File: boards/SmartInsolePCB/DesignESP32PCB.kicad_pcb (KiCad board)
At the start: 2 copper layers, 54 parts, among them J1 Conn_01x02_Pin, J10 Conn_01x02_Pin, J11 Conn_01x02_Pin, J12 Conn_01x02_Pin, J2 Conn_01x02_Pin, J3 Conn_01x06_Pin, J4 Conn_01x02_Pin, J5 Conn_01x02_Pin, J6 Conn_01x02_Pin, J7 Conn_01x02_Pin, J8 Conn_01x02_Pin, J9 Conn_01x02_Pin, SW1 SW_Push, SW2 SW_Push, U1 ESP32-S3-MINI-1-N8, U2 D3V3XA4B10LP, U3 TLV75801PDRV, U4 SN74LVC1G14DBV, U5 SN74LVC1G14DBV, U6 MPU-6050

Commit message: finished schematic
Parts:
- added SW3: SW_Push, Button_Switch_SMD:SW_Push_1P1T_NO_CK_PTS125Sx43PSMTR, F.Cu at (49.2, 75.9)
- added SW4: SW_Push, Button_Switch_SMD:SW_Push_1P1T_NO_CK_PTS125Sx43PSMTR, F.Cu at (49.2, 89.4)
- added U7: ESP32-S3-WROOM-1, RF_Module:ESP32-S3-WROOM-1, F.Cu at (186.1, 62.7)
- BOOT1, RESET1: footprint Button_Switch_SMD:SW_SPST_PTS810 -> Button_Switch_SMD:SW_Push_1P1T_NO_CK_PTS125Sx43PSMTR
- C5, C8: value 0.1uF -> 1uF
- J3: value Conn_01x06_Pin -> PJS008U-3000-0; footprint Connector_PinHeader_1.00mm:PinHeader_1x06_P1.00mm_Vertical -> SmartInsolePCB:PJS008U30000
- R14, R15: value 1k -> 10k
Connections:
- C5 pad 1: Net-(C5-Pad1) -> /End Hike
- C8 pad 1: Net-(C8-Pad1) -> /Start Hike
- J3 pad 1: GND -> /CS
- J3 pad 2: /GPIO48 -> /MOSI
- J3 pad 3: /GPIO45 -> GND
- J3 pad 4: /GPIO47 -> /3V3
- J3 pad 5: /CS -> /SCLK
- J3 pad 6: +3.3V -> GND
- R10 pad 1: /GPIO12 -> /GPIO3
- R11 pad 1: /GPIO13 -> /GPIO6
- R12 pad 1: /GPIO14 -> /GPIO7
- R13 pad 1: /GPIO15 -> /GPIO8
- R14 pad 2: +3.3V -> /End Hike
- R15 pad 1: Net-(C8-Pad1) -> Net-(R15-Pad1)
- R15 pad 2: Net-(R14-Pad1) -> /Start Hike
- R18 pad 1: /GPIO16 -> /GPIO11
- R19 pad 1: /GPIO17 -> /GPIO12
- R20 pad 1: /GPIO18 -> /GPIO21
- R21 pad 1: /GPIO19 -> /GPIO38
- R22 pad 1: /GPIO20 -> /GPIO47
- R3 pad 1: /GPIO10 -> /GPIO1
- R9 pad 1: /GPIO11 -> /GPIO2
- SW1 pad 2: Net-(R16-Pad1) -> Net-(R14-Pad1)
- SW2 pad 2: Net-(R14-Pad1) -> Net-(R15-Pad1)
- U6 pad 23: /GPIO35 -> /SCL_6050
- U6 pad 24: /GPIO34 -> /SDA_6050

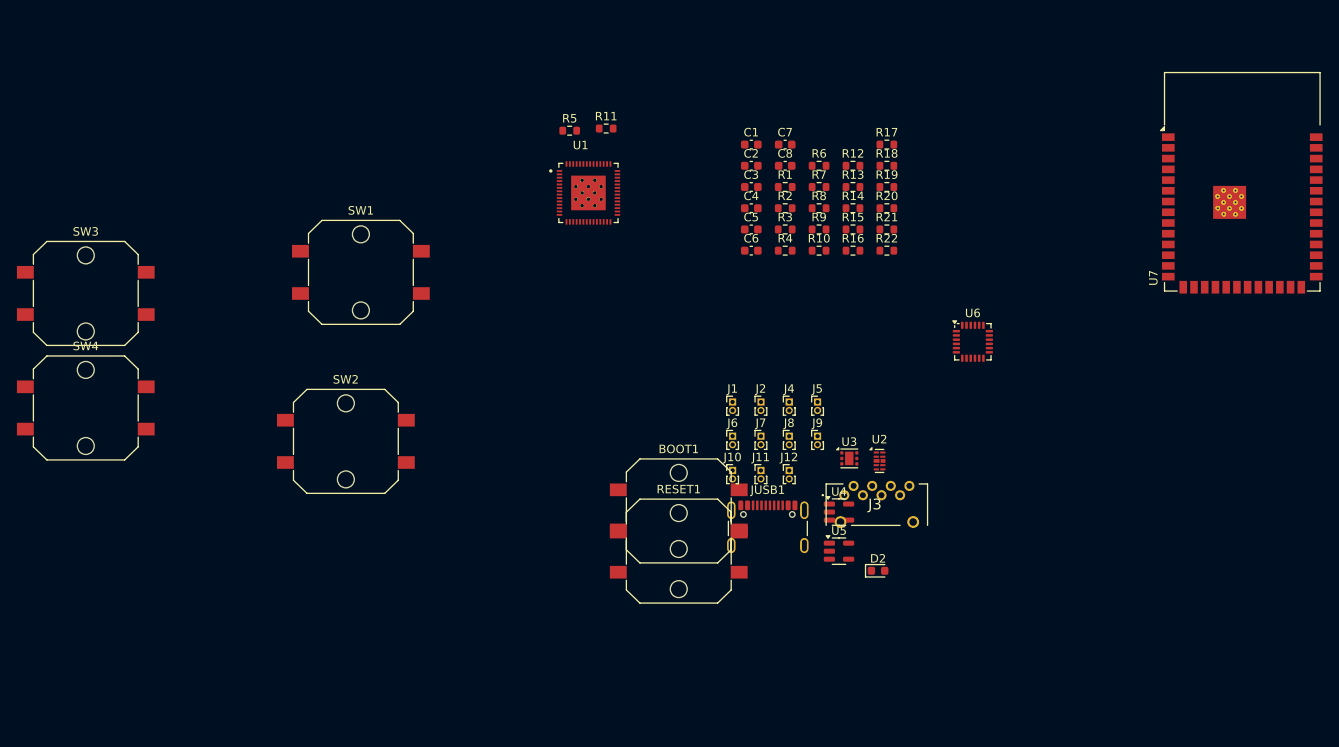
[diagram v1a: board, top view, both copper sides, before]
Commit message: finished all PCB connections
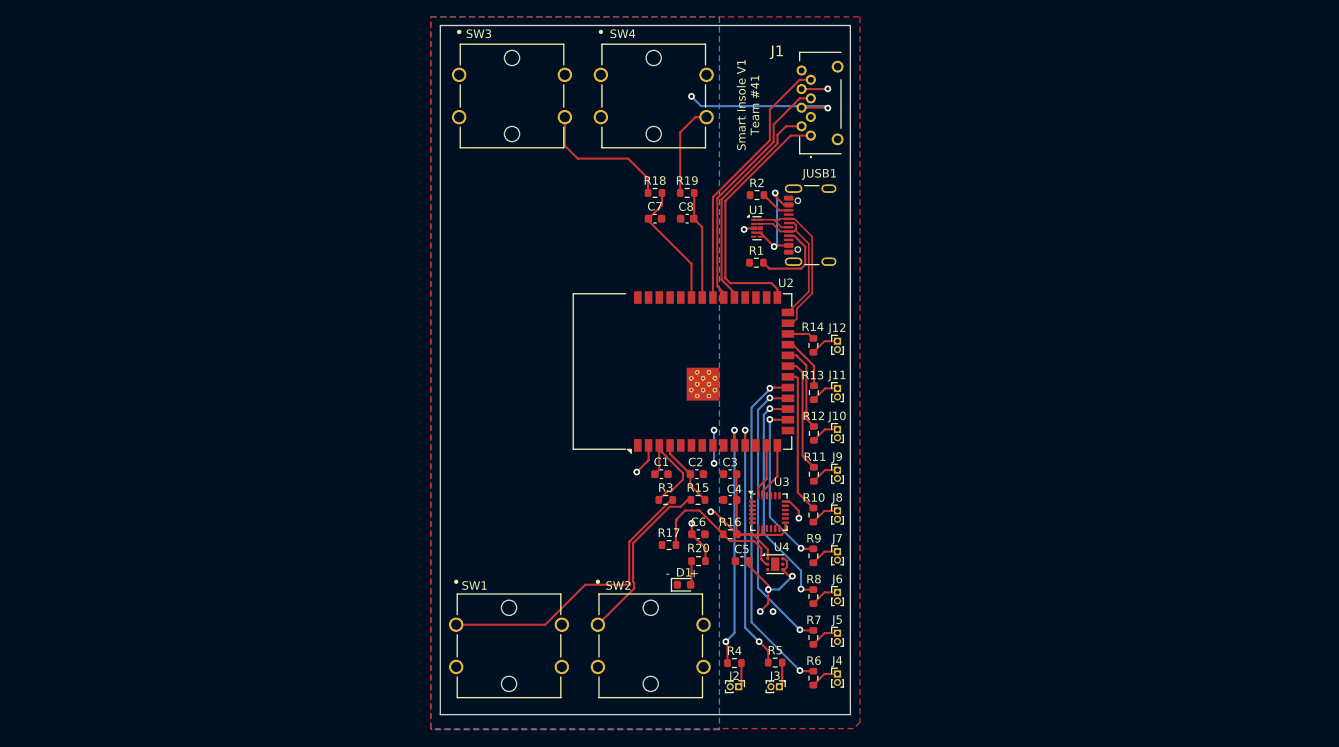
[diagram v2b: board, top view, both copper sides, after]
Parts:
- removed BOOT1, RESET1: ~, Button_Switch_SMD:SW_Push_1P1T_NO_CK_PTS125Sx43PSMTR
- removed D2: LED, LED_SMD:LED_0603_1608Metric
- removed R21, R22: 1k, Resistor_SMD:R_0603_1608Metric
- removed U5: SN74LVC1G14DBV, Package_TO_SOT_SMD:SOT-23-5
- removed U6: MPU-6050, Sensor_Motion:InvenSense_QFN-24_4x4mm_P0.5mm
- removed U7: ESP32-S3-WROOM-1, RF_Module:ESP32-S3-WROOM-1
- added D1: LED, LED_SMD:LED_0603_1608Metric, F.Cu at (120.0, 110.4)
- C2: value 10uF -> 0.1uF
- C4: value 0.1uF -> 10uF
- C5: value 1uF -> 10uF
- C7: value 10uF -> 1uF
- J1: value Conn_01x02_Pin -> PJS008U-3000-0; footprint Connector_PinHeader_1.00mm:PinHeader_1x02_P1.00mm_Vertical -> SmartInsolePCB:PJS008U30000
- J3: value PJS008U-3000-0 -> Conn_01x02_Pin; footprint SmartInsolePCB:PJS008U30000 -> Connector_PinHeader_1.00mm:PinHeader_1x02_P1.00mm_Vertical
- R14, R4, R5: value 10k -> 1k
- R15: value 10k -> 1.0k
- R16: value 1k -> 1M
- R17: value 1k -> 200k
- R18, R19: value 1k -> 5k
- R20: value 1k -> 5.1k
- R3: value 1k -> 1.0k
- R6: value 1M -> 1k
- R7: value 200k -> 1k
- R8: value 5.1k -> 1k
- SW1, SW2, SW3, SW4: value SW_Push -> B3F-4000; footprint Button_Switch_SMD:SW_Push_1P1T_NO_CK_PTS125Sx43PSMTR -> SmartInsolePCB:SW_B3F-4000_OMR
- U1: value ESP32-S3-MINI-1-N8 -> D3V3XA4B10LP; footprint RF_Module:IC_ESP32-S3 -> Package_DFN_QFN:Diodes_UDFN-10_1.0x2.5mm_P0.5mm
- U2: value D3V3XA4B10LP -> ESP32-S3-WROOM-1; footprint Package_DFN_QFN:Diodes_UDFN-10_1.0x2.5mm_P0.5mm -> RF_Module:ESP32-S3-WROOM-1
- U3: value TLV75801PDRV -> MPU-6050; footprint Package_SON:WSON-6-1EP_2x2mm_P0.65mm_EP1x1.6mm -> Sensor_Motion:InvenSense_QFN-24_4x4mm_P0.5mm
- U4: value SN74LVC1G14DBV -> TLV75801PDRV; footprint Package_TO_SOT_SMD:SOT-23-5 -> Package_SON:WSON-6-1EP_2x2mm_P0.65mm_EP1x1.6mm
- moved SW4 72.6 mm to (110.2, 50.0)
- moved R5 67.5 mm to (130.8, 119.6)
- moved R6 60.6 mm to (135.3, 121.4), turned to -90 degrees
- moved R17 53.9 mm to (118.2, 105.7)
- moved R7 53.3 mm to (135.3, 116.6), turned to -90 degrees
- moved SW3 51.2 mm to (93.4, 50.0)
- moved R4 49.2 mm to (126.0, 119.6)
- moved R11 47.7 mm to (135.4, 97.3), turned to -90 degrees
- moved R20 47.3 mm to (121.7, 107.6), turned to 180 degrees
- moved R8 46.0 mm to (135.3, 111.8), turned to -90 degrees
- moved SW1 43.2 mm to (93.1, 115.1)
- moved C1 40.4 mm to (117.3, 97.3)
- moved C5 39.3 mm to (126.9, 107.6), turned to 180 degrees
- moved R9 38.6 mm to (135.3, 106.9), turned to -90 degrees
- moved JUSB1 37.3 mm to (136.1, 67.8), turned to 90 degrees
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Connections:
- C1 pad 1: /3V3 -> /ESP32_EN
- C2 pad 1: /3V3 -> /GPIO4
- C3 pad 1: /ESP32_EN -> /3V3
- C4 pad 1: /GPIO0 -> /3V3
- C5 pad 1: /End Hike -> /POWER FROM BATTERY
- C6 pad 1: /5VUSB -> /3V3
- C7 pad 1: /3V3 -> /End Hike
- J1 pad 1: Net-(J1-Pin_1) -> /CS
- J1 pad 2: GND -> /MOSI
- J3 pad 1: /CS -> Net-(J3-Pin_1)
- J3 pad 2: /MOSI -> GND
- R1 pad 1: Net-(JUSB1-CC2) -> Net-(JUSB1-CC1)
- R10 pad 1: /GPIO3 -> /GPIO11
- R10 pad 2: Net-(J4-Pin_1) -> Net-(J8-Pin_1)
- R11 pad 1: /GPIO6 -> /GPIO12
- R11 pad 2: Net-(J5-Pin_1) -> Net-(J9-Pin_1)
- R12 pad 1: /GPIO7 -> /GPIO21
- R12 pad 2: Net-(J6-Pin_1) -> Net-(J10-Pin_1)
- R13 pad 1: /GPIO8 -> /GPIO10
- R13 pad 2: Net-(J7-Pin_1) -> Net-(J11-Pin_1)
- R14 pad 1: Net-(R14-Pad1) -> /GPIO47
- R14 pad 2: /End Hike -> Net-(J12-Pin_1)
- R15 pad 2: /Start Hike -> /GPIO4
- R16 pad 1: Net-(R16-Pad1) -> Net-(U4-FB)
- R16 pad 2: +3.3V -> /3V3
- R17 pad 1: Net-(C5-Pad1) -> GND
- R17 pad 2: Net-(R16-Pad1) -> Net-(U4-FB)
- R18 pad 1: /GPIO11 -> Net-(R18-Pad1)
- R18 pad 2: Net-(J8-Pin_1) -> /End Hike
- R19 pad 1: /GPIO12 -> Net-(R19-Pad1)
- R19 pad 2: Net-(J9-Pin_1) -> /Start Hike
- R2 pad 1: Net-(JUSB1-CC1) -> Net-(JUSB1-CC2)
- R20 pad 1: /GPIO21 -> /3V3
- R20 pad 2: Net-(J10-Pin_1) -> Net-(D1-A)
- R3 pad 1: /GPIO1 -> /ESP32_EN
- R3 pad 2: Net-(J1-Pin_1) -> Net-(R3-Pad2)
- R4 pad 1: /I2C_SCL -> /GPIO1
- R4 pad 2: /3V3 -> Net-(J2-Pin_1)
- R5 pad 1: /I2C_SDA -> /GPIO2
- R5 pad 2: /3V3 -> Net-(J3-Pin_1)
- R6 pad 1: Net-(U3-FB) -> /GPIO3
- R6 pad 2: /3V3 -> Net-(J4-Pin_1)
- R7 pad 1: GND -> /GPIO6
- R7 pad 2: Net-(U3-FB) -> Net-(J5-Pin_1)
- R8 pad 1: /3V3 -> /GPIO7
- R8 pad 2: Net-(D2-A) -> Net-(J6-Pin_1)
- R9 pad 1: /GPIO2 -> /GPIO8
- R9 pad 2: Net-(J2-Pin_1) -> Net-(J7-Pin_1)
- SW1 pad 1: GND -> Net-(R3-Pad2)
- SW1 pad 2: Net-(R14-Pad1) -> unconnected-(SW1-Pad2)
- SW2 pad 1: GND -> Net-(R15-Pad1)
- SW2 pad 2: Net-(R15-Pad1) -> unconnected-(SW2-Pad2)
- SW3 pad 1: GND -> /3V3
- SW3 pad 2: /GPIO0 -> unconnected-(SW3-Pad2)
- SW4 pad 1: GND -> /3V3
- SW4 pad 2: /ESP32_EN -> unconnected-(SW4-Pad2)
- U1 pad 1: GND -> /USB_P
- U1 pad 10: /GPIO6 -> unconnected-(U1-NC-Pad10)
- U1 pad 2: GND -> /USB_N
- U1 pad 3: /3V3 -> GND
- U1 pad 4: /GPIO0 -> /5VUSB
- U1 pad 5: /GPIO1 -> unconnected-(U1-Pad5)
- U1 pad 6: /GPIO2 -> unconnected-(U1-NC-Pad6)
- U1 pad 7: /GPIO3 -> unconnected-(U1-NC-Pad7)
- U1 pad 8: /GPIO4 -> GND
- U1 pad 9: /GPIO5 -> unconnected-(U1-NC-Pad9)
- U2 pad 1: /USB_P -> GND
- U2 pad 10: unconnected-(U2-NC-Pad10) -> /GPIO1
- U2 pad 2: /USB_N -> /3V3
- U2 pad 3: GND -> /ESP32_EN
- U2 pad 4: /5VUSB -> /GPIO4
- U2 pad 8: GND -> unconnected-(U2-IO15-Pad8)
- U3 pad 1: /3V3 -> unconnected-(U3-CLKIN-Pad1)
- U3 pad 2: Net-(U3-FB) -> unconnected-(U3-NC-Pad2)
- U3 pad 3: GND -> unconnected-(U3-NC-Pad3)
- U3 pad 4: /5VUSB -> unconnected-(U3-NC-Pad4)
- U3 pad 6: /5VUSB -> unconnected-(U3-AUX_DA-Pad6)
- U3 pad 7: GND -> unconnected-(U3-AUX_CL-Pad7)
- U4 pad 1: unconnected-(U4-NC-Pad1) -> /3V3
- U4 pad 2: Net-(C5-Pad1) -> Net-(U4-FB)
- U4 pad 4: /Start Hike -> /POWER FROM BATTERY
- U4 pad 5: +3.3V -> unconnected-(U4-DNC-Pad5)
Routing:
- net /3V3: track 0.00 -> 54.6 mm, vias 0 -> 5
- net /GPIO3: track 0.00 -> 40.5 mm, vias 0 -> 2
- net Net-(R3-Pad2): track 0.00 -> 34.9 mm
- net /GPIO6: track 0.00 -> 33.8 mm, vias 0 -> 2
- net /MISO: track 0.00 -> 31.3 mm
- net /GPIO2: track 0.00 -> 30.4 mm, vias 0 -> 2
- net /CS: track 0.00 -> 30.1 mm
- net /GPIO1: track 0.00 -> 29.9 mm, vias 0 -> 2
- net /SCLK: track 0.00 -> 29.2 mm
- net /GPIO7: track 0.00 -> 27.1 mm, vias 0 -> 2
- net /MOSI: track 0.00 -> 25.9 mm
- net /USB_P: track 0.00 -> 21.7 mm
- net Net-(R15-Pad1): track 0.00 -> 20.4 mm
- net /GPIO8: track 0.00 -> 20.4 mm, vias 0 -> 2
- net /USB_N: track 0.00 -> 18.4 mm
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- added copper zone on B.Cu, net /3V3
- added copper zone on F.Cu, net GND
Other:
- board outline added: 48.5 x 81.5 mm
- board text added: "+"
- board text added: "-"
- board text added: "Smart Insole V1 Team #41"

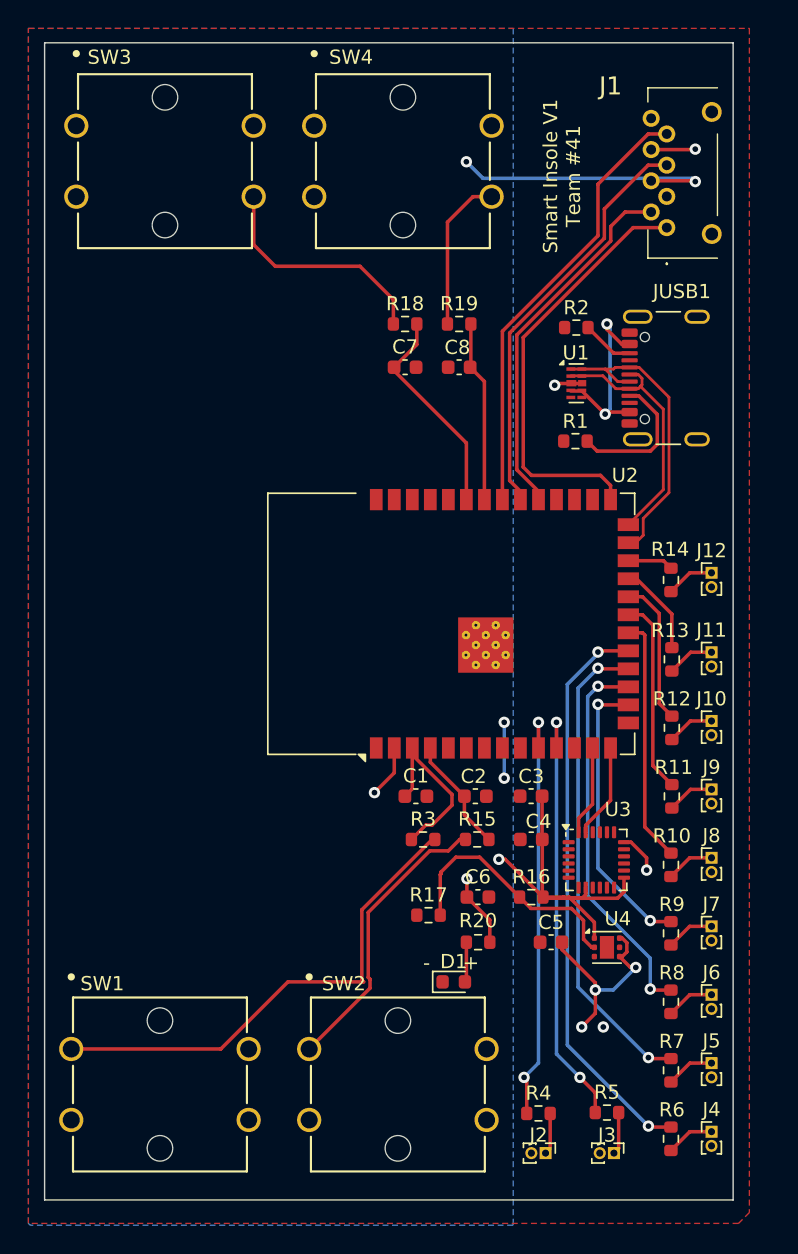
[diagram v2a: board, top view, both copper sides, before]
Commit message: down from 200 to 43 errors
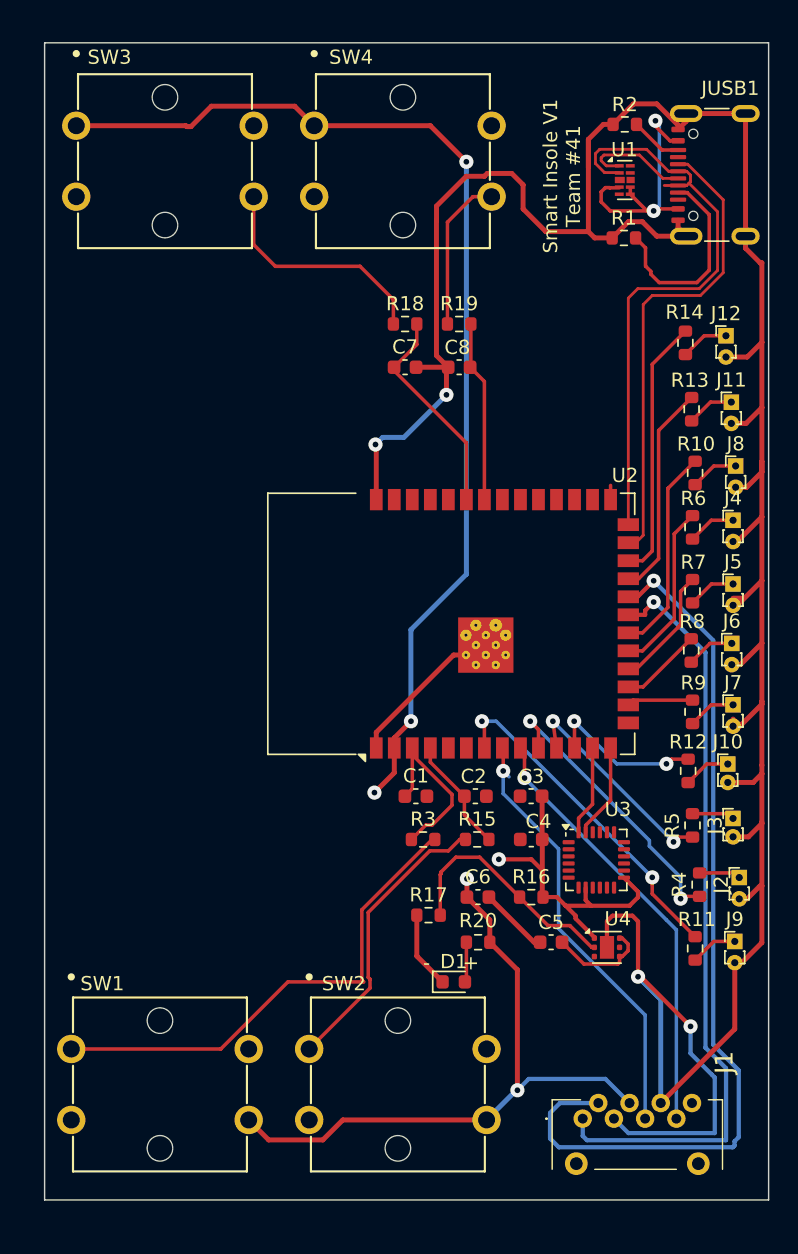
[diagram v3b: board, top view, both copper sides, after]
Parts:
- moved J1 67.6 mm to (132.7, 121.1), turned to 0 degrees
- moved J4 43.1 mm to (139.7, 77.8)
- moved R6 43.1 mm to (136.8, 78.3)
- moved J5 33.8 mm to (139.7, 82.3)
- moved R7 33.8 mm to (136.8, 82.8)
- moved R10 27.7 mm to (137.0, 74.5)
- moved J8 27.7 mm to (139.9, 74.0)
- moved J3 25.0 mm to (139.7, 98.8), turned to 0 degrees
- moved J6 24.8 mm to (139.6, 86.5)
- moved R8 24.8 mm to (136.7, 87.0)
- moved J2 23.7 mm to (140.1, 103.0), turned to 0 degrees
- moved R5 21.1 mm to (136.8, 99.3), turned to 90 degrees
- moved R4 19.7 mm to (137.3, 103.5), turned to 90 degrees
- moved J11 17.7 mm to (139.6, 69.5)
- moved R13 17.7 mm to (136.8, 70.0)
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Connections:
- U1 pad 6: unconnected-(U1-NC-Pad6) -> /5VUSB
- U1 pad 7: unconnected-(U1-NC-Pad7) -> /5VUSB
- U2 pad 12: unconnected-(U2-IO8-Pad12) -> /GPIO21
- U2 pad 21: /GPIO12 -> /CS
- U2 pad 22: /GPIO21 -> /MOSI
- U2 pad 27: /CS -> unconnected-(U2-IO0-Pad27)
- U2 pad 31: /MOSI -> unconnected-(U2-IO38-Pad31)
- U2 pad 32: /SCLK -> unconnected-(U2-IO39-Pad32)
- U2 pad 33: /MISO -> unconnected-(U2-IO40-Pad33)
- U2 pad 7: unconnected-(U2-IO7-Pad7) -> /GPIO12
- U2 pad 8: unconnected-(U2-IO15-Pad8) -> /SCLK
- U2 pad 9: unconnected-(U2-IO16-Pad9) -> /MISO
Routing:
- net GND: track 11.9 -> 235.2 mm, vias 6 -> 4
- net /3V3: track 54.6 -> 147.4 mm, vias 5 -> 6
- net /MOSI: track 25.9 -> 64.0 mm, vias 0 -> 1
- net /GPIO3: track 40.5 -> 12.0 mm, vias 2 -> 0
- net /GPIO6: track 33.8 -> 8.51 mm, vias 2 -> 0
- net /USB_N: track 18.4 -> 42.7 mm
- net /CS: track 30.1 -> 54.1 mm, vias 0 -> 1
- net /GPIO7: track 27.1 -> 5.84 mm, vias 2 -> 0
- net /USB_P: track 21.7 -> 41.3 mm
- net /GPIO8: track 20.4 -> 4.66 mm, vias 2 -> 0
- net /GPIO47: track 3.22 -> 18.4 mm
- net /GPIO2: track 30.4 -> 15.7 mm
- net /GPIO12: track 13.8 -> 24.4 mm, vias 0 -> 2
- net /GPIO1: track 29.9 -> 20.5 mm
- net /GPIO10: track 6.47 -> 15.0 mm
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- removed copper zone on B.Cu, net /3V3
- removed copper zone on F.Cu, net GND
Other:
- board size 48.5 x 81.5 mm -> 51 x 81.5 mm

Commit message: schematic and pcb updates
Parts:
- added J13: Conn_01x05_Socket, Connector_PinHeader_1.00mm:PinHeader_1x05_P1.00mm_Vertical_SMD_Pin1Left, F.Cu at (139.2, 113.8)
- added JP1: SolderJumper_3_Open, Jumper:SolderJumper-3_P2.0mm_Open_TrianglePad1.0x1.5mm, F.Cu at (161.8, 95.2)
- added Q1: SS8050-G, SmartInsolePCB:TRAN_SS8050-G_CIP, F.Cu at (134.2, 111.3)
- added Q2: SS8050-G, SmartInsolePCB:TRAN_SS8050-G_CIP, F.Cu at (134.2, 115.2)
- added R21: 1.0k, Resistor_SMD:R_0603_1608Metric, F.Cu at (152.0, 89.8)
- added R22: 1k, Resistor_SMD:R_0603_1608Metric, F.Cu at (152.0, 92.3)
- added R23: 10k, Resistor_SMD:R_0603_1608Metric, F.Cu at (130.9, 111.9)
- added R24: 10k, Resistor_SMD:R_0603_1608Metric, F.Cu at (127.7, 115.1)
- added R25: 10k, Resistor_SMD:R_0603_1608Metric, F.Cu at (130.9, 115.1)
- added R26: 10k, Resistor_SMD:R_0603_1608Metric, F.Cu at (127.7, 111.7)
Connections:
- C1 pad 1: /ESP32_EN -> Net-(C1-Pad1)
- C2 pad 1: /GPIO4 -> Net-(C2-Pad1)
- R15 pad 1: Net-(R15-Pad1) -> /GPIO0_STRAPPING
- R15 pad 2: /GPIO4 -> /3V3
- R3 pad 2: Net-(R3-Pad2) -> /3V3
- SW1 pad 1: Net-(R3-Pad2) -> GND
- SW1 pad 3: unconnected-(SW1-Pad3) -> Net-(C1-Pad1)
- SW1 pad 4: /3V3 -> /ESP32_EN
- SW2 pad 1: Net-(R15-Pad1) -> GND
- SW2 pad 3: unconnected-(SW2-Pad3) -> Net-(C2-Pad1)
- SW2 pad 4: /3V3 -> /GPIO0_STRAPPING
- U1 pad 6: /5VUSB -> unconnected-(U1-NC-Pad6)
- U1 pad 7: /5VUSB -> unconnected-(U1-NC-Pad7)
- U2 pad 15: unconnected-(U2-IO3-Pad15) -> /GPIO3_STRAPPING
- U2 pad 16: /GPIO8 -> /GPIO46_STRAPPING
- U2 pad 27: unconnected-(U2-IO0-Pad27) -> /GPIO0_STRAPPING
- U2 pad 36: /RXD -> /RX
- U2 pad 37: /TXD -> /TX
- U2 pad 4: /GPIO4 -> unconnected-(U2-IO4-Pad4)
- U2 pad 6: unconnected-(U2-IO6-Pad6) -> /GPIO8
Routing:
- net GND: track 235.2 -> 18.6 mm, vias 4 -> 0
- net /3V3: track 147.4 -> 51.0 mm, vias 6 -> 4
- net /RX: track 0.00 -> 63.2 mm, vias 0 -> 2
- net /TX: track 0.00 -> 58.2 mm, vias 0 -> 2
- net /ESP32_EN: track 12.7 -> 69.9 mm, vias 0 -> 2
- net Net-(C1-Pad1): track 0.00 -> 38.0 mm
- net /GPIO0_STRAPPING: track 0.00 -> 36.1 mm, vias 0 -> 3
- net Net-(R3-Pad2): track 34.9 -> 0.00 mm
- net Net-(C2-Pad1): track 0.00 -> 28.3 mm
- net Net-(R15-Pad1): track 20.4 -> 0.00 mm
- net /RTS: track 0.00 -> 17.7 mm, vias 0 -> 2
- net Net-(Q1-Pad3): track 0.00 -> 12.5 mm
- net /DTR: track 0.00 -> 10.4 mm
- net /GPIO4: track 8.15 -> 0.00 mm
- net Net-(Q2-Pad3): track 0.00 -> 6.52 mm
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- added copper zone on B.Cu, net /3V3
- added copper zone on F.Cu, net GND
